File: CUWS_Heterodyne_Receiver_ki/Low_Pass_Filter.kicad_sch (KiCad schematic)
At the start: 0 parts

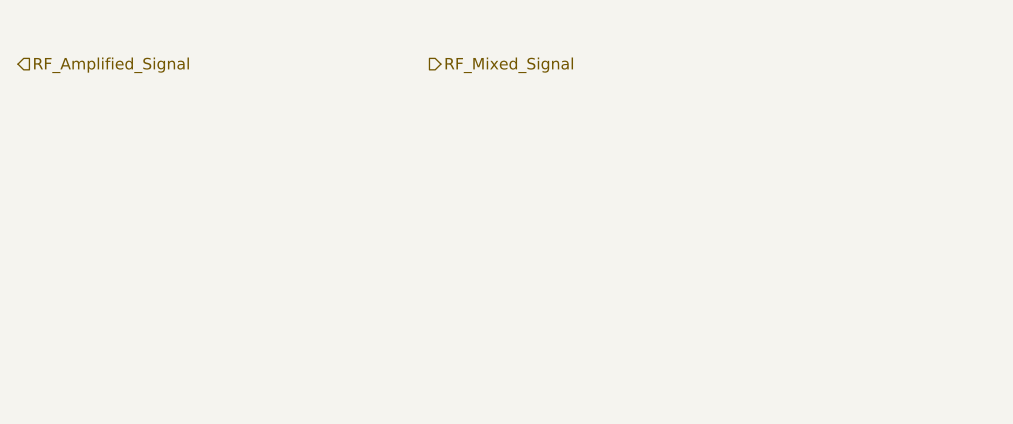
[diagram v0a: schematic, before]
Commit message: Finalised first draft of top hierarchy
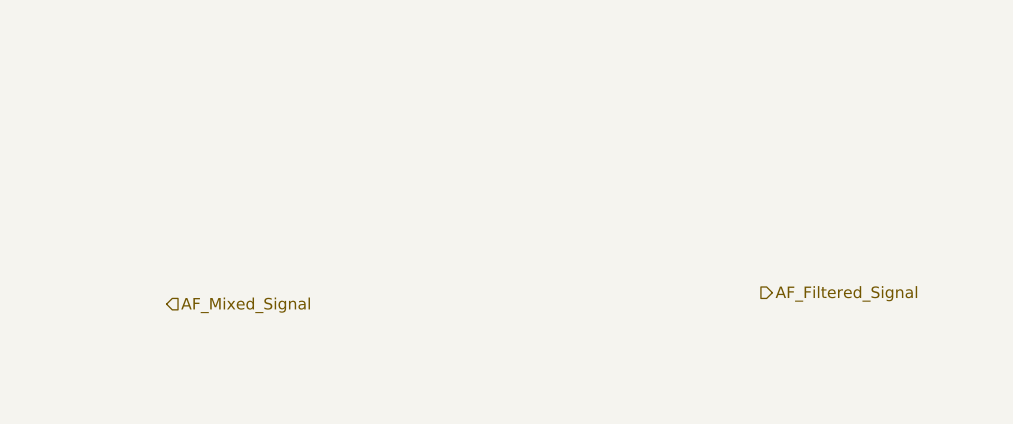
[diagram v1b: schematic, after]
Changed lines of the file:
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@@
 	(generator_version "8.0")
 	(paper "A4")
-	(hierarchical_label "RF_Amplified_Signal"
-		(shape input)
-		(at 50.8 81.28 0)
+	(hierarchical_label "AF_Filtered_Signal"
+		(shape output)
+		(at 133.35 106.68 0)
 		(fields_autoplaced yes)
 		(effects
@@
 		)
 	)
-	(hierarchical_label "RF_Mixed_Signal"
-		(shape output)
-		(at 96.52 81.28 0)
+	(hierarchical_label "AF_Mixed_Signal"
+		(shape input)
+		(at 67.31 107.95 0)
 		(fields_autoplaced yes)
 		(effects

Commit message: Copied Low Pass Filter
OP27 opamp based filter/amp
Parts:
- added C1: 3p, Capacitor_THT:CP_Axial_L10.0mm_D4.5mm_P15.00mm_Horizontal, symbol Device:C
- added R1: 10k, Resistor_THT:R_Axial_DIN0309_L9.0mm_D3.2mm_P12.70mm_Horizontal, symbol Device:R
- added R2: 10M, Resistor_THT:R_Axial_DIN0309_L9.0mm_D3.2mm_P12.70mm_Horizontal, symbol Device:R
- added U1: OP07, OP07DP:DIP794W45P254L959H508Q8, symbol Amplifier_Operational:OP07
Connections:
- net AF_Filtered_Signal: now also C1.2, R2.2, U1.6
- net AF_Mixed_Signal: now also U1.3 (+)
- new net: C1.1, R1.2, R2.1, U1.2 (-)
- new net Ground: R1.1
- no-connect marks 0 -> 2

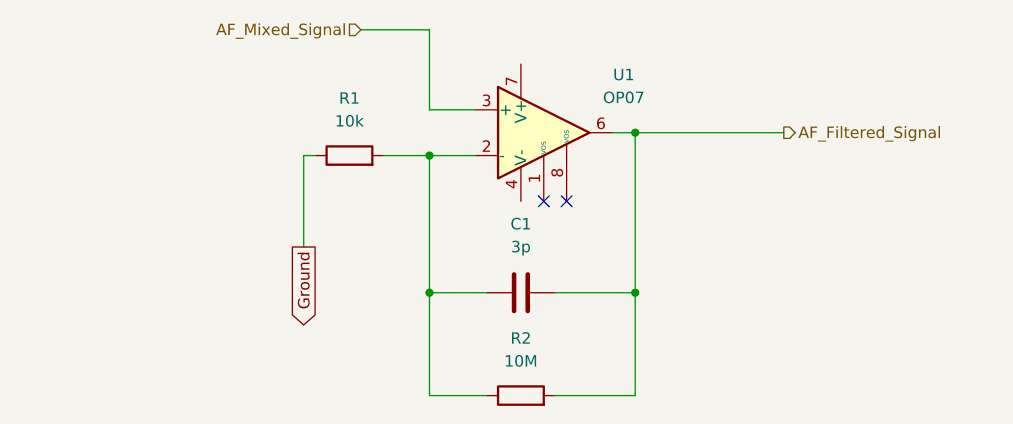
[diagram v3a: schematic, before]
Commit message: Fixing AF Amp stages
Fixed the low pass filter and voltage OpAmp circuit, followed by a push-pull current amp.
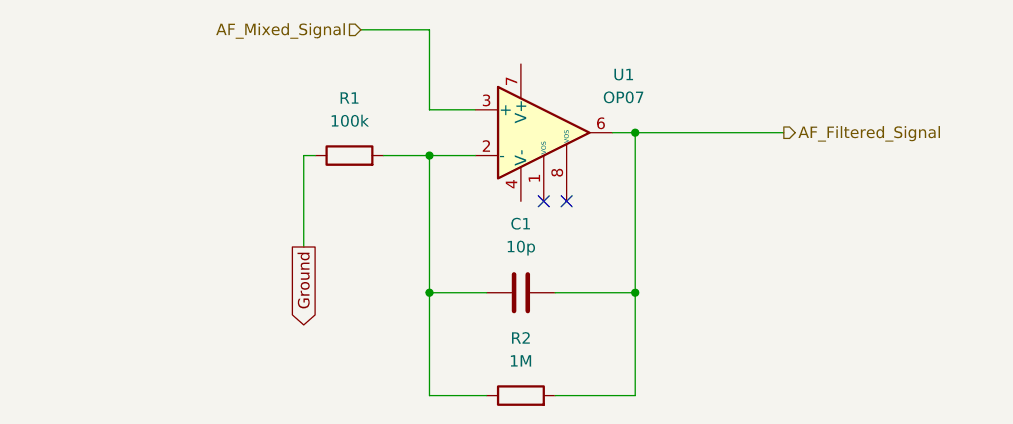
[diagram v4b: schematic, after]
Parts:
- C1: value 3p -> 10p
- R1: value 10k -> 100k
- R2: value 10M -> 1M
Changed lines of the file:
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@@
 			)
 		)
-		(property "Value" "10k"
+		(property "Value" "100k"
 			(at 87.63 87.63 90)
 			(effects
@@
 			(project "CUWS_Heterodyne_Receiver_ki"
 				(path "/b54120a5-f5cb-4b8f-8dd9-cbf19c375861/16591230-9530-4c97-8e5f-0b22d93769a7"
+					(reference "R1")
+					(unit 1)
+				)
+			)
+			(project "Low_Pass_Filter"
+				(path "/e81ff986-986c-4863-b415-962fe1b09d2e"
 					(reference "R1")
 					(unit 1)
@@
 				)
 			)
+			(project "Low_Pass_Filter"
+				(path "/e81ff986-986c-4863-b415-962fe1b09d2e"
+					(reference "U1")
+					(unit 1)
+				)
+			)
 		)
 	)
@@
 			)
 		)
-		(property "Value" "10M"
+		(property "Value" "1M"
 			(at 106.68 114.3 90)
 			(effects
@@
 			(project "CUWS_Heterodyne_Receiver_ki"
 				(path "/b54120a5-f5cb-4b8f-8dd9-cbf19c375861/16591230-9530-4c97-8e5f-0b22d93769a7"
+					(reference "R2")
+					(unit 1)
+				)
+			)
+			(project "Low_Pass_Filter"
+				(path "/e81ff986-986c-4863-b415-962fe1b09d2e"
 					(reference "R2")
 					(unit 1)
@@
 			)
 		)
-		(property "Value" "3p"
+		(property "Value" "10p"
 			(at 106.68 101.6 90)
 			(effects
@@
 				)
 			)
-		)
-	)
+			(project "Low_Pass_Filter"
+				(path "/e81ff986-986c-4863-b415-962fe1b09d2e"
+					(reference "C1")
+					(unit 1)
+				)
+			)
+		)
+	)
+	(sheet_instances
+		(path "/"
+			(page "1")
+		)
+	)
+	(embedded_fonts no)
 )
